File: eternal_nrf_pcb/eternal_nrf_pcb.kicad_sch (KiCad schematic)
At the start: 55 parts, among them J1 Conn_01x07_Pin, Q1 IRLML6244, Q2 IRLML6402, SW1 SW_Push, U1 BQ25504, U2 nRF52810-QCxx, U3 DRV5032DU, U4 SHTC3, Y1 Crystal_GND24, Y2 Crystal

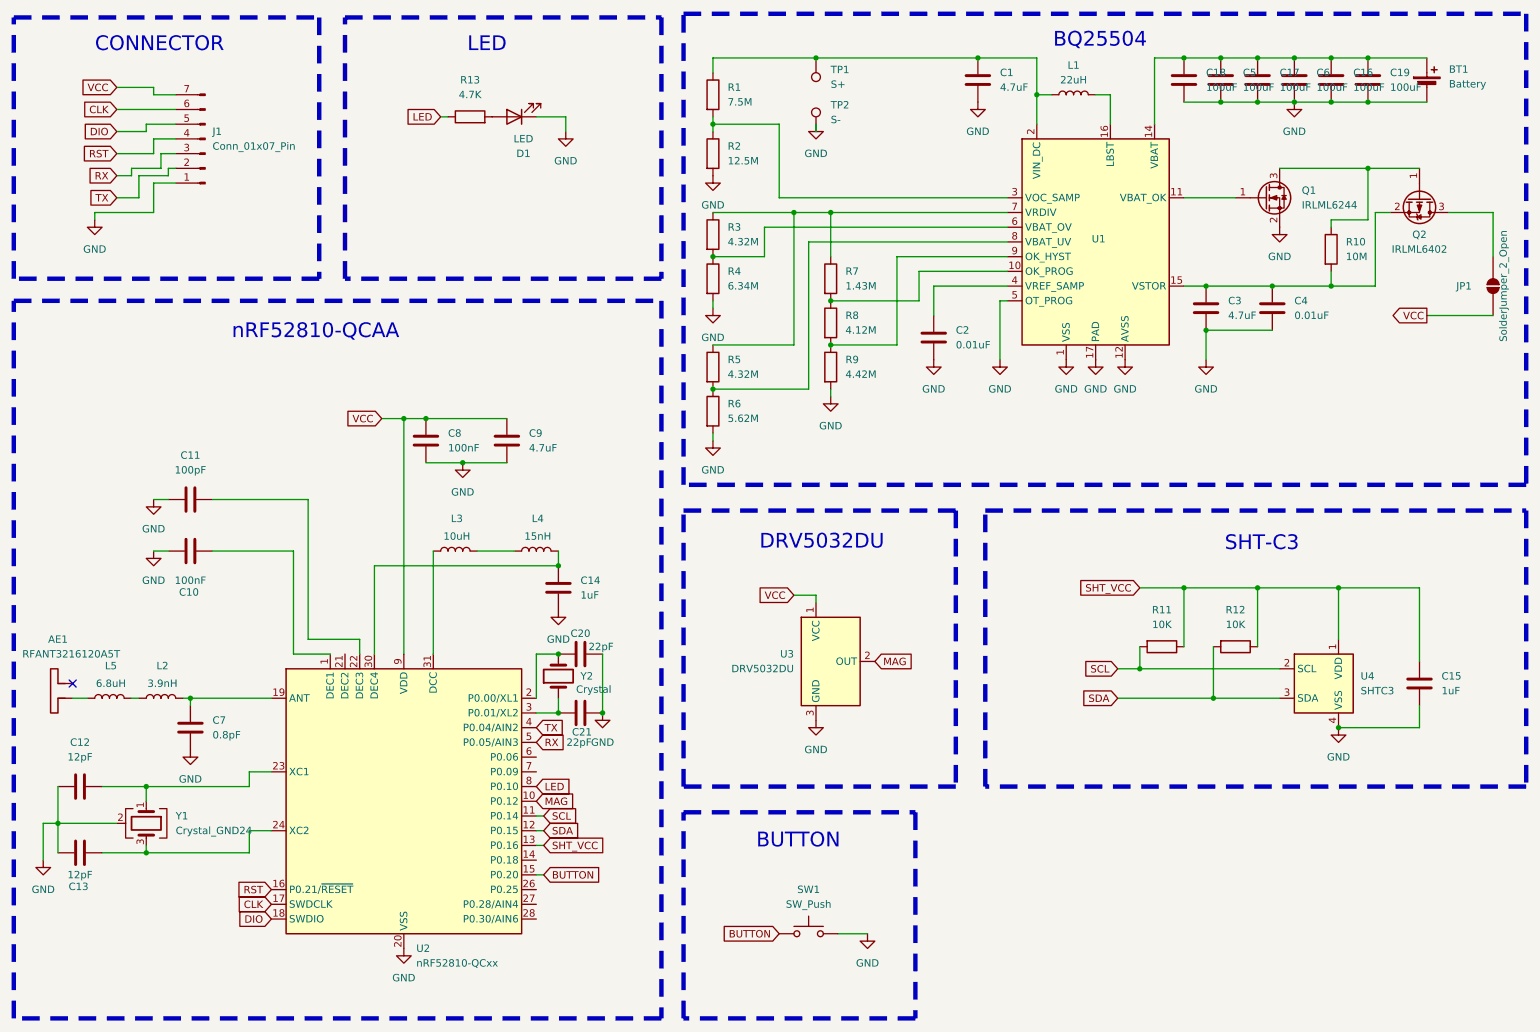
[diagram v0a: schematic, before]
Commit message: increase trace width
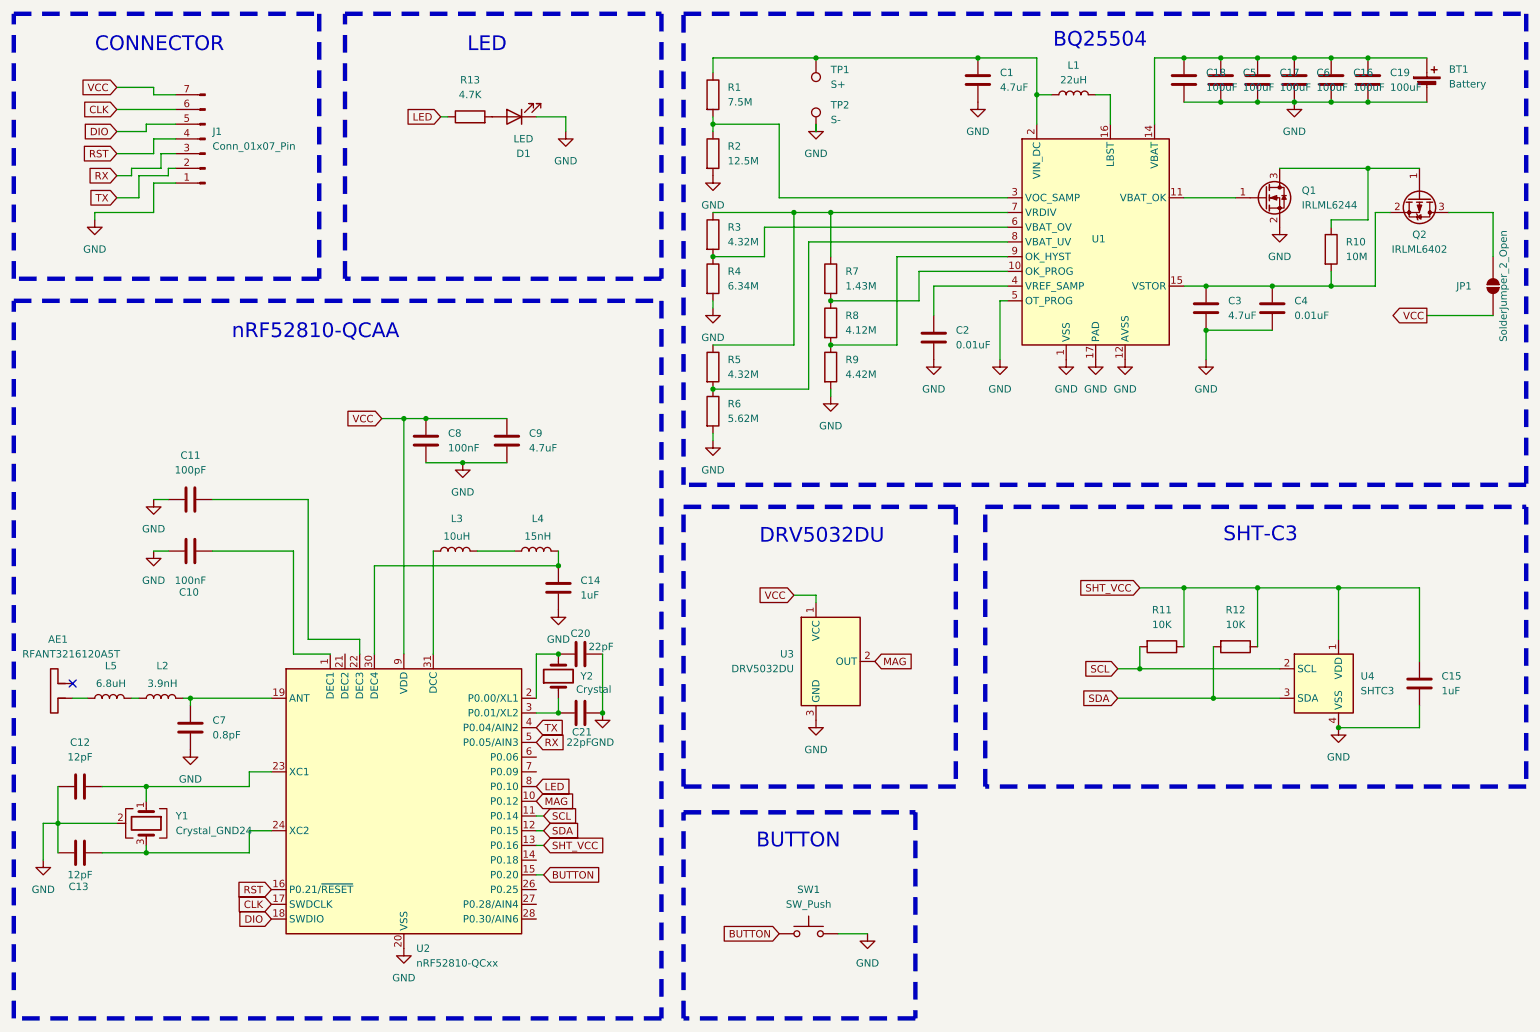
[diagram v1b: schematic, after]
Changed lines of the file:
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@@
 	)
 	(rectangle
-		(start 185.42 104.775)
+		(start 185.42 104.14)
 		(end 278.765 152.4)
 		(stroke
@@
 	)
 	(rectangle
-		(start 17.78 19.685)
+		(start 17.78 19.05)
 		(end 70.485 64.77)
 		(stroke
@@
 	)
 	(rectangle
-		(start 74.93 19.685)
+		(start 74.93 19.05)
 		(end 129.54 64.77)
 		(stroke
@@
 	)
 	(rectangle
-		(start 133.35 104.775)
+		(start 133.35 104.14)
 		(end 180.34 152.4)
 		(stroke
@@
 	(text "DRV5032DU"
 		(exclude_from_sim no)
-		(at 157.226 110.236 0)
+		(at 157.226 109.22 0)
 		(effects
 			(font
@@
 	(text "SHT-C3\n"
 		(exclude_from_sim no)
-		(at 233.172 110.49 0)
+		(at 232.918 108.966 0)
 		(effects
 			(font

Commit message: add production file
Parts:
- added C22: 100nF, Capacitor_SMD:C_0402_1005Metric_Pad0.74x0.62mm_HandSolder, symbol Device:C
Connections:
- net GND: now also C22.2
- net VCC: now also C22.1
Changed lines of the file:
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@@
 	)
 	(rectangle
-		(start 185.42 104.14)
+		(start 184.15 104.14)
 		(end 278.765 152.4)
 		(stroke
@@
 	)
 	(rectangle
-		(start 133.35 156.845)
+		(start 133.35 156.21)
 		(end 173.355 192.405)
 		(stroke
@@
 	)
 	(rectangle
-		(start 74.93 19.05)
+		(start 74.295 19.05)
 		(end 129.54 64.77)
 		(stroke
@@
 	)
 	(junction
+		(at 102.87 96.52)
+		(diameter 0)
+		(color 0 0 0 0)
+	)
+	(junction
 		(at 245.11 66.04)
 		(diameter 0)
@@
 	)
 	(junction
+		(at 102.87 88.9)
+		(diameter 0)
+		(color 0 0 0 0)
+	)
+	(junction
 		(at 138.43 60.96)
 		(diameter 0)
@@
 	(wire
 		(pts
+			(xy 102.87 96.52) (xy 115.57 96.52)
+		)
+		(stroke
+			(width 0)
+			(type default)
+		)
+	)
+	(wire
+		(pts
 			(xy 25.4 158.75) (xy 35.56 158.75)
 		)
@@
 		)
 	)
+	(wire
+		(pts
+			(xy 102.87 88.9) (xy 115.57 88.9)
+		)
+		(stroke
+			(width 0)
+			(type default)
+		)
+	)
 	(global_label "SDA"
 		(shape input)
@@
 					(unit 1)
 				)
+			)
+		)
+	)
+	(symbol
+		(lib_id "Device:C")
+		(at 115.57 92.71 0)
+		(unit 1)
+		(body_style 1)
+		(exclude_from_sim no)
+		(in_bom yes)
+		(on_board yes)
+		(in_pos_files yes)
+		(dnp no)
+		(fields_autoplaced yes)
+		(property "Reference" "C22"
+			(at 119.38 91.4399 0)
+			(show_name no)
+			(do_not_autoplace no)
+			(effects
+				(font
+					(size 1.27 1.27)
+				)
+				(justify left)
+			)
+		)
+		(property "Value" "100nF"
+			(at 119.38 93.9799 0)
+			(show_name no)
+			(do_not_autoplace no)
+			(effects
+				(font
+					(size 1.27 1.27)
+				)
+				(justify left)
+			)
+		)
+		(property "Footprint" "Capacitor_SMD:C_0402_1005Metric_Pad0.74x0.62mm_HandSolder"
+			(at 116.5352 96.52 0)
+			(hide yes)
+			(show_name no)
+			(do_not_autoplace no)
+			(effects
+				(font
+					(size 1.27 1.27)
+				)
+			)
+		)
+		(property "Datasheet" ""
+			(at 115.57 92.71 0)
+			(hide yes)
+			(show_name no)
+			(do_not_autoplace no)
+			(effects
+				(font
+					(size 1.27 1.27)
+				)
+			)
+		)
+		(property "Description" "Unpolarized capacitor"
+			(at 115.57 92.71 0)
+			(hide yes)
+			(show_name no)
+			(do_not_autoplace no)
+			(effects
+				(font
+					(size 1.27 1.27)
+				)
+			)
+		)
+		(pin "2"
+		)
+		(pin "1"
+		)
+		(instances
+			(project "eternal_nrf_pcb"
+				(path "/debe71e3-c42e-4b38-900f-830a3de6dac1"
+					(reference "C22")
+					(unit 1)
+				)

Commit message: fix bugs
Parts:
- R3, R5: value 4.32M -> 4.02M
- R4: value 6.34M -> 5.90M
- R6: value 5.62M -> 5.90M
- R7: value 1.43M -> 2.26M
- R8: value 4.12M -> 3.32M
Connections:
- net at R7.2, R8.1: now also U1.9 (OK_HYST); no longer U1.10 (OK_PROG)
- net at R8.2, R9.1: now also U1.10 (OK_PROG); no longer U1.9 (OK_HYST)
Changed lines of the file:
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@@
 	)
 	(junction
+		(at 158.75 68.58)
+		(diameter 0)
+		(color 0 0 0 0)
+	)
+	(junction
 		(at 234.95 66.04)
 		(diameter 0)
@@
 	)
 	(junction
-		(at 158.75 76.2)
-		(diameter 0)
-		(color 0 0 0 0)
-	)
-	(junction
 		(at 246.38 142.24)
 		(diameter 0)
@@
 	)
 	(junction
-		(at 158.75 68.58)
+		(at 238.76 26.67)
 		(diameter 0)
 		(color 0 0 0 0)
 	)
 	(junction
-		(at 238.76 26.67)
+		(at 158.75 76.2)
 		(diameter 0)
 		(color 0 0 0 0)
@@
 	(wire
 		(pts
+			(xy 158.75 76.2) (xy 168.91 76.2)
+		)
+		(stroke
+			(width 0)
+			(type default)
+		)
+	)
+	(wire
+		(pts
 			(xy 85.09 88.9) (xy 88.9 88.9)
 		)
@@
 	(wire
 		(pts
-			(xy 170.18 76.2) (xy 158.75 76.2)
-		)
-		(stroke
-			(width 0)
-			(type default)
-		)
-	)
-	(wire
-		(pts
 			(xy 149.86 38.1) (xy 138.43 38.1)
 		)
@@
 	(wire
 		(pts
-			(xy 173.99 68.58) (xy 158.75 68.58)
-		)
-		(stroke
-			(width 0)
-			(type default)
-		)
-	)
-	(wire
-		(pts
 			(xy 66.04 111.76) (xy 66.04 129.54)
 		)
@@
 	(wire
 		(pts
-			(xy 173.99 63.5) (xy 173.99 68.58)
-		)
-		(stroke
-			(width 0)
-			(type default)
-		)
-	)
-	(wire
-		(pts
 			(xy 219.71 118.11) (xy 219.71 128.27)
 		)
@@
 	(wire
 		(pts
-			(xy 189.23 63.5) (xy 173.99 63.5)
+			(xy 189.23 63.5) (xy 172.72 63.5)
 		)
 		(stroke
@@
 	(wire
 		(pts
+			(xy 170.18 68.58) (xy 158.75 68.58)
+		)
+		(stroke
+			(width 0)
+			(type default)
+		)
+	)
+	(wire
+		(pts
 			(xy 214.63 26.67) (xy 219.71 26.67)
 		)
@@
 	(wire
 		(pts
-			(xy 33.02 163.83) (xy 40.64 163.83)
+			(xy 168.91 71.12) (xy 168.91 76.2)
 		)
 		(stroke
@@
 	(wire
 		(pts
-			(xy 260.35 138.43) (xy 260.35 142.24)
+			(xy 33.02 163.83) (xy 40.64 163.83)
 		)
 		(stroke
@@
 	(wire
 		(pts
-			(xy 138.43 83.82) (xy 154.94 83.82)
+			(xy 260.35 138.43) (xy 260.35 142.24)
 		)
 		(stroke
@@
 	(wire
 		(pts
-			(xy 138.43 91.44) (xy 138.43 92.71)
+			(xy 138.43 83.82) (xy 154.94 83.82)
 		)
 		(stroke
@@
 	(wire
 		(pts
-			(xy 170.18 60.96) (xy 170.18 76.2)
+			(xy 138.43 91.44) (xy 138.43 92.71)
 		)
 		(stroke
@@
 	(wire
 		(pts
+			(xy 172.72 71.12) (xy 168.91 71.12)
+		)
+		(stroke
+			(width 0)
+			(type default)
+		)
+	)
+	(wire
+		(pts
 			(xy 194.31 26.67) (xy 194.31 33.02)
 		)
@@
 	(wire
 		(pts
+			(xy 170.18 60.96) (xy 170.18 68.58)
+		)
+		(stroke
+			(width 0)
+			(type default)
+		)
+	)
+	(wire
+		(pts
 			(xy 158.75 53.34) (xy 158.75 60.96)
 		)
@@
 	(wire
 		(pts
+			(xy 172.72 63.5) (xy 172.72 71.12)
+		)
+		(stroke
+			(width 0)
+			(type default)
+		)
+	)
+	(wire
+		(pts
 			(xy 58.42 149.86) (xy 62.23 149.86)
 		)
@@
 			)
 		)
-		(property "Value" "4.12M"
+		(property "Value" "3.32M"
 			(at 161.29 73.6599 0)
 			(show_name no)
@@
 			)
 		)
-		(property "Value" "5.62M"
+		(property "Value" "5.90M"
 			(at 140.97 88.8999 0)
 			(show_name no)
@@
 			)
 		)
-		(property "Value" "4.32M"
+		(property "Value" "4.02M"
 			(at 140.97 81.2799 0)
 			(show_name no)
@@
 			)
 		)
-		(property "Value" "4.32M"
+		(property "Value" "4.02M"
 			(at 140.97 58.4199 0)
 			(show_name no)
@@
 			)
 		)
-		(property "Value" "1.43M"
+		(property "Value" "2.26M"
 			(at 161.29 66.0399 0)
 			(show_name no)
@@
 			)
 		)
-		(property "Value" "6.34M"
+		(property "Value" "5.90M"
 			(at 140.97 66.0399 0)
 			(show_name no)

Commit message: final production file
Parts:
- L5: value 6.8uH -> 6.8nH
- R13: value 4.7K -> 1K
- SW1: value SW_Push -> TSA002A3216A
- U2: value nRF52810-QCxx -> nRF52810-QCAA
- Y1: value Crystal_GND24 -> S3232000081040
- Y2: value Crystal -> X1A0001410003
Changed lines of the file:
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@@
 			)
 		)
-		(property "Value" "4.7K"
+		(property "Value" "1K"
 			(at 96.52 33.02 90)
 			(show_name no)
@@
 			)
 		)
-		(property "Value" "Crystal"
-			(at 114.808 135.636 90)
+		(property "Value" "X1A0001410003"
+			(at 113.284 135.636 90)
 			(show_name no)
 			(do_not_autoplace no)
@@
 			)
 		)
-		(property "Value" "Crystal_GND24"
+		(property "Value" "S3232000081040"
 			(at 45.72 160.0199 90)
 			(show_name no)
@@
 			)
 		)
-		(property "Value" "6.8uH"
+		(property "Value" "6.8nH"
 			(at 34.544 134.62 90)
 			(show_name no)
@@
 			)
 		)
-		(property "Value" "nRF52810-QCxx"
+		(property "Value" "nRF52810-QCAA"
 			(at 87.2333 182.88 0)
 			(show_name no)
@@
 			)
 		)
-		(property "Value" "SW_Push"
+		(property "Value" "TSA002A3216A"
 			(at 154.94 172.72 0)
 			(show_name no)
